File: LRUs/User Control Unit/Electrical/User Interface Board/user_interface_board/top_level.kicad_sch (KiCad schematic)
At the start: 13 parts, among them J1 S3B-PH-K-S, J10 S4B-PH-K-S, J11 S4B-PH-K-S, J12 S4B-PH-K-S, J13 S12B-PH-K-S, J2 S3B-PH-K-S, J3 S3B-PH-K-S, J4 S3B-PH-K-S, J5 S2B-PH-K-S, J6 S2B-PH-K-S, J7 S2B-PH-K-S, J8 S4B-PH-K-S, J9 S4B-PH-K-S

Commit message: Commit
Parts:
- added R92, R93: 10k, footprints:R_0603_1608Metric, symbol Device:R_Small_US
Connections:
- net +3V3: now also J8.1 (Pin_1), R92.1, R93.1; no longer J13.1 (Pin_1)
- net GND: now also J1.3 (Pin_3), J2.3 (Pin_3), J3.3 (Pin_3), J4.3 (Pin_3), J8.4 (Pin_4), J9.4 (Pin_4)
- net +5V: now reaches J10.1 (Pin_1)
- net +5V: now also J11.1 (Pin_1), J12.1 (Pin_1), J13.1 (Pin_1)
- net LED driver/OUT0: now reaches J10.2 (Pin_2)
- net LED driver/OUT1: now reaches J10.3 (Pin_3)
- net LED driver/OUT2: now reaches J10.4 (Pin_4)
- net at J13.10 (Pin_10): now also J2.2 (Pin_2), J3.1 (Pin_1), J4.1 (Pin_1)
- net at J13.11 (Pin_11): now also J3.2 (Pin_2)
- net at J13.12 (Pin_12): now also J4.2 (Pin_2)
- net I2C_SDA: now reaches J13.5 (Pin_5)
- net I2C_SDA: now also J8.3 (Pin_3)
- net I2C_SCL: now reaches J13.6 (Pin_6)
- net I2C_SCL: now also J8.2 (Pin_2)
- net launch circuit/ARMED_STAT: now reaches J13.7 (Pin_7)
- net launch circuit/LAUNCH_STAT: now reaches J13.8 (Pin_8)
- net at J13.9 (Pin_9): now also J1.2 (Pin_2)
- net launch circuit/SAFE_LED+: now reaches J5.1 (Pin_1)
- net launch circuit/SAFE_LED-: now reaches J5.2 (Pin_2)
- net launch circuit/ARM_SW-: now reaches J6.2 (Pin_2)
- net at J2.1 (Pin_1): now also R93.2
- net at J1.1 (Pin_1): now also R92.2
- net LED driver/OUT3: now reaches J11.2 (Pin_2)
- net LED driver/OUT4: now reaches J11.3 (Pin_3)
- net LED driver/OUT5: now reaches J11.4 (Pin_4)
- net LED driver/OUT6: now reaches J12.2 (Pin_2)
- net LED driver/OUT7: now reaches J12.3 (Pin_3)
- net LED driver/OUT8: now reaches J12.4 (Pin_4)
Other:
- added sheet LED driver (LED_driver.kicad_sch)
- sheet launch circuit ports: added ARMED_LED+, ARMED_LED-, ARMED_STAT, ARM_SW-, BUTTON+, BUTTON_C, BUTTON_NO, LAUNCH_STAT, SAFE_LED+, SAFE_LED-; removed none
- note added: "COOL"
- note added: "FILL"
- note added: "ON --- OFF"
- note added: "VALVE ARM"
- note added: "VENT"
- moved on the sheet: J1, J13, J2, J3, J4, J5, J6, J7, J9

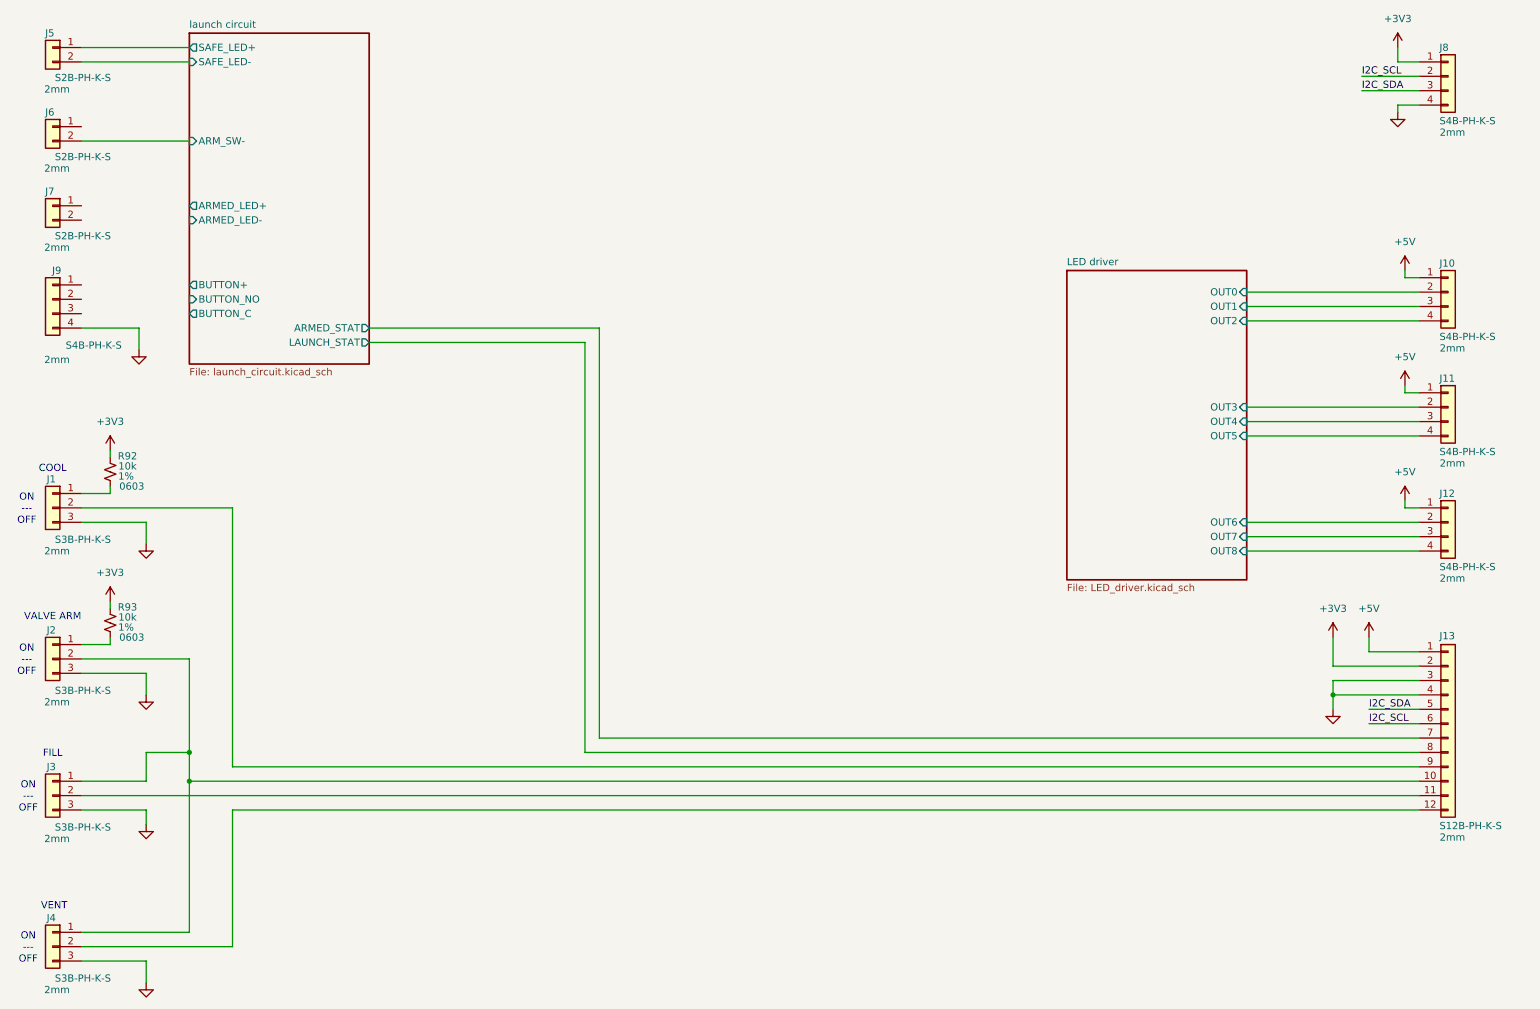
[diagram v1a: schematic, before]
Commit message: interface board schematic
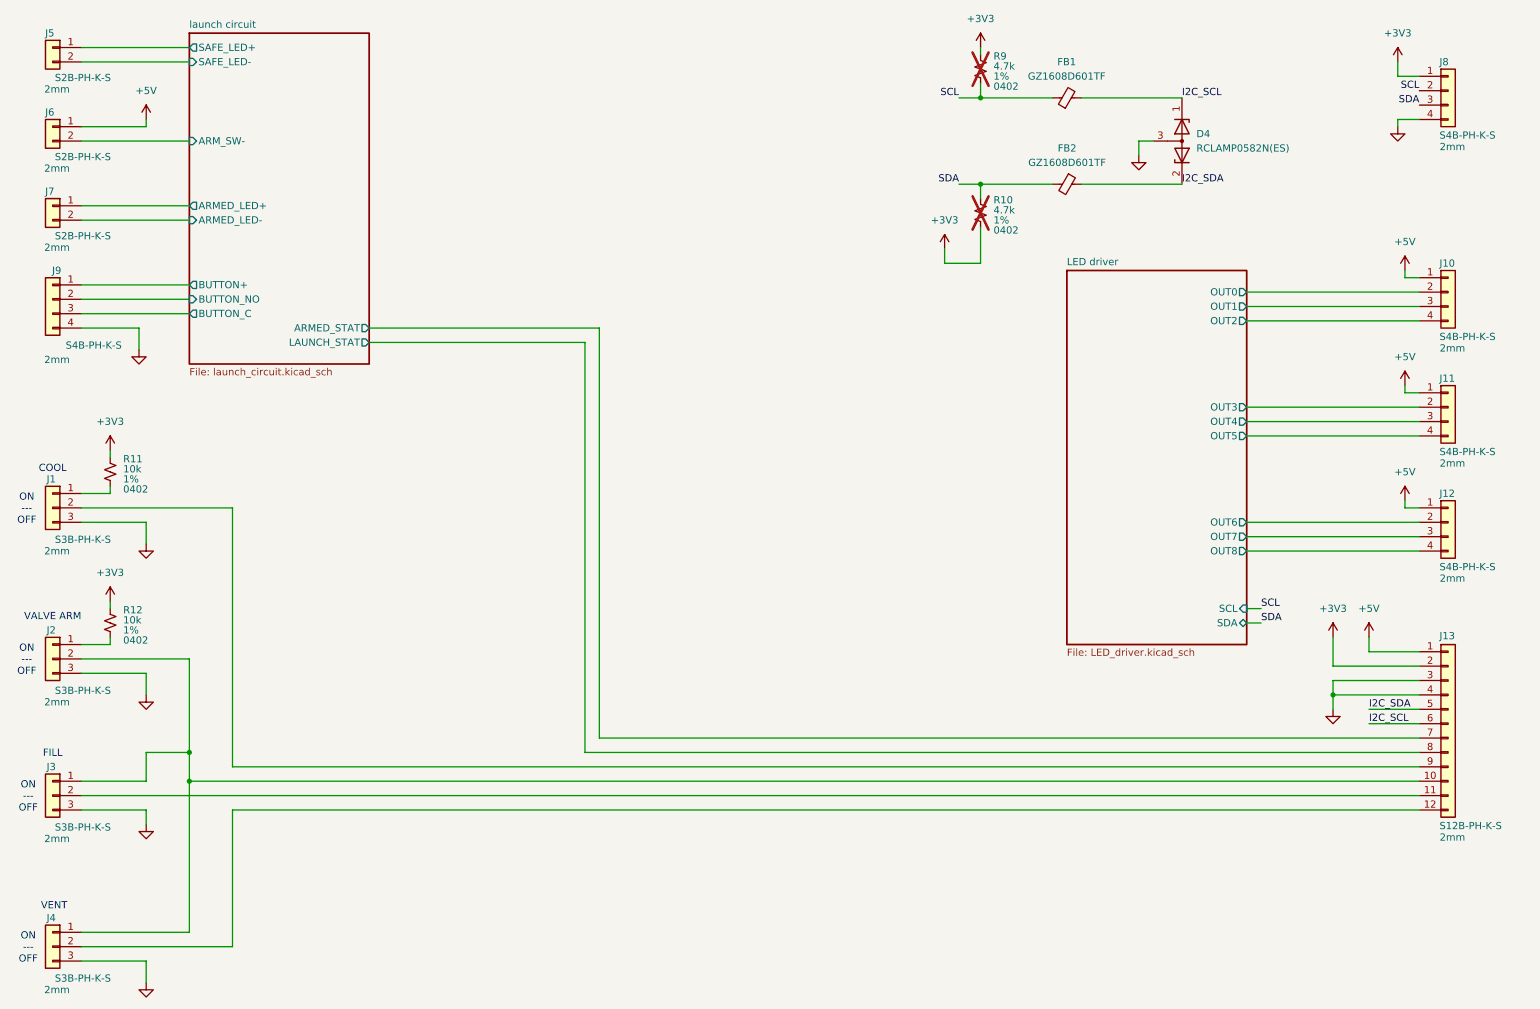
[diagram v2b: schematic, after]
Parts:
- removed R92, R93: 10k, footprints:R_0603_1608Metric, symbol Device:R_Small_US
- added D4: RCLAMP0582N(ES), Project Library:SON40P100X120X65-6N, symbol Project Library:RCLAMP0582N(ES)
- added FB1, FB2: GZ1608D601TF, Inductor_SMD:L_0603_1608Metric, symbol Device:FerriteBead_Small
- added R10, R9: 4.7k, Resistor_SMD:R_0402_1005Metric, symbol Device:R_Small_US
- added R11, R12: 10k, Resistor_SMD:R_0402_1005Metric, symbol Device:R_Small_US
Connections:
- net +3V3: now also R10.2, R11.1, R12.1, R9.1
- net +5V: now also J6.1 (Pin_1)
- net GND: now also D4.3
- net I2C_SCL: now also D4.1, FB1.2; no longer J8.2 (Pin_2)
- net I2C_SDA: now also D4.2, FB2.1; no longer J8.3 (Pin_3)
- net launch circuit/ARMED_LED+: now also J7.1 (Pin_1)
- net launch circuit/ARMED_LED-: now also J7.2 (Pin_2)
- net launch circuit/BUTTON+: now also J9.1 (Pin_1)
- net launch circuit/BUTTON_C: now also J9.3 (Pin_3)
- net launch circuit/BUTTON_NO: now also J9.2 (Pin_2)
- net at J2.1 (Pin_1): now also R12.2
- net at J1.1 (Pin_1): now also R11.2
- new net SCL: FB1.1, J8.2 (Pin_2), R9.2
- new net SDA: FB2.2, J8.3 (Pin_3), R10.1
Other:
- sheet LED driver ports: added SCL, SDA; removed none
- moved on the sheet: J8

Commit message: interface pcb
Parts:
- D4: JLCPCB Part # C46970803 -> (none)
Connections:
- net GND: now also D4.4
- net I2C_SCL: now also D4.6
- net I2C_SDA: now also D4.5
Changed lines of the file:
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@@
+	)
+	(symbol
+		(lib_id "Project Library:RCLAMP0582N(ES)")
+		(at 219.71 36.83 270)
+		(unit 1)
+		(body_style 1)
+		(exclude_from_sim no)
+		(in_bom yes)
+		(on_board yes)
+		(in_pos_files yes)
+		(dnp no)
+		(fields_autoplaced yes)
+		(property "Reference" "D4"
+			(at 222.25 35.5599 90)
+			(show_name no)
+			(do_not_autoplace no)
+			(effects
+				(font
+					(size 1.27 1.27)
+				)
+				(justify left)
+			)
+		)
+		(property "Value" "RCLAMP0582N(ES)"
+			(at 222.25 38.0999 90)
+			(show_name no)
+			(do_not_autoplace no)
+			(effects
+				(font
+					(size 1.27 1.27)
+				)
+				(justify left)
+			)
+		)
+		(property "Footprint" "Project Library:SON40P100X120X65-6N"
+			(at 219.71 36.83 0)
+			(hide yes)
+			(show_name no)
+			(do_not_autoplace no)
+			(effects
+				(font
+					(size 1.27 1.27)
+				)
+			)
+		)
+		(property "Datasheet" ""
+			(at 219.71 36.83 0)
+			(hide yes)
+			(show_name no)
+			(do_not_autoplace no)
+			(effects
+				(font
+					(size 1.27 1.27)
+				)
+			)
+		)
+		(property "Description" ""
+			(at 219.71 36.83 0)
+			(hide yes)
+			(show_name no)
+			(do_not_autoplace no)
+			(effects
+				(font
+					(size 1.27 1.27)
+				)
+			)
+		)
+		(pin "6"
+		)
+		(pin "5"
+		)
+		(pin "3"
+		)
+		(pin "2"
+		)
+		(pin "1"
+		)
+		(pin "4"
+		)
+		(instances
+			(project "user_interface_board"
+				(path "/5c9cf600-f97e-40e0-a9fc-86e24261d606"
+					(reference "D4")
+					(unit 1)
+				)
+			)
+		)
 	)
 	(symbol
@@
 					(unit 1)
 				)
-			)
-		)
-	)
-	(symbol
-		(lib_id "Project Library:RCLAMP0582N(ES)")
-		(at 219.71 36.83 270)
-		(unit 1)
-		(body_style 1)
-		(exclude_from_sim no)
-		(in_bom yes)
-		(on_board yes)
-		(in_pos_files yes)
-		(dnp no)
-		(fields_autoplaced yes)
-		(property "Reference" "D4"
-			(at 222.25 35.5599 90)
-			(show_name no)
-			(do_not_autoplace no)
-			(effects
-				(font
-					(size 1.27 1.27)
-				)
-				(justify left)
-			)
-		)
-		(property "Value" "RCLAMP0582N(ES)"
-			(at 222.25 38.0999 90)
-			(show_name no)
-			(do_not_autoplace no)
-			(effects
-				(font
-					(size 1.27 1.27)
-				)
-				(justify left)
-			)
-		)
-		(property "Footprint" "Project Library:SON40P100X120X65-6N"
-			(at 219.71 36.83 0)
-			(hide yes)
-			(show_name no)
-			(do_not_autoplace no)
-			(effects
-				(font
-					(size 1.27 1.27)
-				)
-			)
-		)
-		(property "Datasheet" ""
-			(at 219.71 36.83 0)
-			(hide yes)
-			(show_name no)
-			(do_not_autoplace no)
-			(effects
-				(font
-					(size 1.27 1.27)
-				)
-			)
-		)
-		(property "Description" ""
-			(at 219.71 36.83 0)
-			(hide yes)
-			(show_name no)
-			(do_not_autoplace no)
-			(effects
-				(font
-					(size 1.27 1.27)
-				)
-			)
-		)
-		(property "JLCPCB Part #" "C46970803"
-			(at 219.71 36.83 0)
-			(hide yes)
-			(show_name no)
-			(do_not_autoplace no)
-			(effects
-				(font
-					(size 1.27 1.27)
-				)
-			)
-		)
-		(pin "2"
-		)
-		(pin "3"
-		)
-		(pin "1"
-		)
-		(instances
-			(project "user_interface_board"
-				(path "/5c9cf600-f97e-40e0-a9fc-86e24261d606"
-					(reference "D4")
-					(unit 1)
-				)

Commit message: fix drc & add level shifter
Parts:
- R11, R12: JLCPCB Part # C17414 -> C25744
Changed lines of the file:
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@@
+	)
+	(symbol
+		(lib_id "Device:R_Small_US")
+		(at 30.48 121.92 0)
+		(unit 1)
+		(body_style 1)
+		(exclude_from_sim no)
+		(in_bom yes)
+		(on_board yes)
+		(in_pos_files yes)
+		(dnp no)
+		(property "Reference" "R12"
+			(at 32.766 119.634 0)
+			(show_name no)
+			(do_not_autoplace no)
+			(effects
+				(font
+					(size 1.27 1.27)
+				)
+				(justify left)
+			)
+		)
+		(property "Value" "10k"
+			(at 32.766 121.412 0)
+			(show_name no)
+			(do_not_autoplace no)
+			(effects
+				(font
+					(size 1.27 1.27)
+				)
+				(justify left)
+			)
+		)
+		(property "Footprint" "Resistor_SMD:R_0402_1005Metric"
+			(at 30.48 121.92 0)
+			(hide yes)
+			(show_name no)
+			(do_not_autoplace no)
+			(effects
+				(font
+					(size 1.27 1.27)
+				)
+			)
+		)
+		(property "Datasheet" ""
+			(at 30.48 121.92 0)
+			(hide yes)
+			(show_name no)
+			(do_not_autoplace no)
+			(effects
+				(font
+					(size 1.27 1.27)
+				)
+			)
+		)
+		(property "Description" "10kΩ 50V 62.5mW Thick Film Resistor ±1%"
+			(at 30.48 121.92 0)
+			(hide yes)
+			(show_name no)
+			(do_not_autoplace no)
+			(effects
+				(font
+					(size 1.27 1.27)
+				)
+			)
+		)
+		(property "Tolerance" "1%"
+			(at 32.766 123.19 0)
+			(show_name no)
+			(do_not_autoplace no)
+			(effects
+				(font
+					(size 1.27 1.27)
+				)
+				(justify left)
+			)
+		)
+		(property "JLCPCB Part #" "C25744"
+			(at 30.48 121.92 0)
+			(hide yes)
+			(show_name no)
+			(do_not_autoplace no)
+			(effects
+				(font
+					(size 1.27 1.27)
+				)
+			)
+		)
+		(property "Footprint_Size" "0402"
+			(at 32.766 124.968 0)
+			(show_name no)
+			(do_not_autoplace no)
+			(effects
+				(font
+					(size 1.27 1.27)
+				)
+				(justify left)
+			)
+		)
+		(pin "1"
+		)
+		(pin "2"
+		)
+		(instances
+			(project "user_interface_board"
+				(path "/5c9cf600-f97e-40e0-a9fc-86e24261d606"
+					(reference "R12")
+					(unit 1)
+				)
+			)
+		)
 	)
 	(symbol
@@
 			)
 		)
-		(property "Description" "10kΩ 125mW 150V Thick Film Resistor ±1%"
+		(property "Description" "10kΩ 50V 62.5mW Thick Film Resistor ±1%"
 			(at 30.48 95.25 0)
 			(hide yes)
@@
 			)
 		)
-		(property "JLCPCB Part #" "C17414"
+		(property "JLCPCB Part #" "C25744"
 			(at 30.48 95.25 0)
 			(hide yes)
@@
 					(unit 1)
 				)
-			)
-		)
-	)
-	(symbol
-		(lib_id "Device:R_Small_US")
-		(at 30.48 121.92 0)
-		(unit 1)
-		(body_style 1)
-		(exclude_from_sim no)
-		(in_bom yes)
-		(on_board yes)
-		(in_pos_files yes)
-		(dnp no)
-		(property "Reference" "R12"
-			(at 32.766 119.634 0)
-			(show_name no)
-			(do_not_autoplace no)
-			(effects
-				(font
-					(size 1.27 1.27)
-				)
-				(justify left)
-			)
-		)
-		(property "Value" "10k"
-			(at 32.766 121.412 0)
-			(show_name no)
-			(do_not_autoplace no)
-			(effects
-				(font
-					(size 1.27 1.27)
-				)
-				(justify left)
-			)
-		)
-		(property "Footprint" "Resistor_SMD:R_0402_1005Metric"
-			(at 30.48 121.92 0)
-			(hide yes)
-			(show_name no)
-			(do_not_autoplace no)
-			(effects
-				(font
-					(size 1.27 1.27)
-				)
-			)
-		)
-		(property "Datasheet" ""
-			(at 30.48 121.92 0)
-			(hide yes)
-			(show_name no)
-			(do_not_autoplace no)
-			(effects
-				(font
-					(size 1.27 1.27)
-				)
-			)
-		)
-		(property "Description" "10kΩ 125mW 150V Thick Film Resistor ±1%"
-			(at 30.48 121.92 0)
-			(hide yes)
-			(show_name no)
-			(do_not_autoplace no)
-			(effects
-				(font
-					(size 1.27 1.27)
-				)
-			)
-		)
-		(property "Tolerance" "1%"
-			(at 32.766 123.19 0)
-			(show_name no)
-			(do_not_autoplace no)
-			(effects
-				(font
-					(size 1.27 1.27)
-				)
-				(justify left)
-			)
-		)
-		(property "JLCPCB Part #" "C17414"
-			(at 30.48 121.92 0)
-			(hide yes)
-			(show_name no)
-			(do_not_autoplace no)
-			(effects
-				(font
-					(size 1.27 1.27)
-				)
-			)
-		)
-		(property "Footprint_Size" "0402"
-			(at 32.766 124.968 0)
-			(show_name no)
-			(do_not_autoplace no)
-			(effects
-				(font
-					(size 1.27 1.27)
-				)
-				(justify left)
-			)
-		)
-		(pin "1"
-		)
-		(pin "2"
-		)
-		(instances
-			(project "user_interface_board"
-				(path "/5c9cf600-f97e-40e0-a9fc-86e24261d606"
-					(reference "R12")
-					(unit 1)
-				)

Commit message: style & add prod files
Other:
- title: (none) -> Top Level
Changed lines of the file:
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@@
 	(generator_version "10.0")
 	(paper "A4")
+	(title_block
+		(title "Top Level")
+		(date "2026-10-26")
+		(rev "A")
+	)
 	(text "ON\n---\nOFF"
 		(exclude_from_sim no)
